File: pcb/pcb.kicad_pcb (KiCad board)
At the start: 2 copper layers, 58 parts, among them J1 Conn_02x10_Odd_Even, J2 Conn_02x03_Counter_Clockwise, Q1 BSS138, Q2 BSS138, Q3 BSS138, Q4 BSS138, SW1 SW_PUSHBUTTON, SW2 SW_PUSHBUTTON, SW3 SW_PUSHBUTTON, SW4 SW_PUSHBUTTON, U1 EFM32GG980, U2 ARDUINO_PYNQ_SHIELD, U3 IMU, U4 lidar, U5 HC-SR04, U6 HC-SR04, Y1 Crystal_GND23

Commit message: start on pcb layout
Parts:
- C1, C10, C2, C3, C4, C5, C6, C7, C8, C9, J2, L1, R5, Y1: moved to B.Cu
- J1: footprint Connector_Multicomp:Multicomp_MC9A22-2034_2x10_P2.54mm_Horizontal -> Connector_Multicomp:Multicomp_MC9A12-2034_2x10_P2.54mm_Vertical
- moved J2 142.8 mm to (117.6, 81.0)
- moved U4 122.4 mm to (94.7, 65.5), turned to 270 degrees
- moved JP9 105.1 mm to (100.3, 106.7), turned to 270 degrees
- moved JP5 105.0 mm to (73.7, 49.5), turned to 90 degrees
- moved JP3 104.6 mm to (78.7, 61.0), turned to 90 degrees
- moved U5 102.7 mm to (170.2, 65.5)
- moved R6 98.8 mm to (165.2, 68.1), turned to 180 degrees
- moved R4 96.7 mm to (127.4, 54.6)
- moved R17 96.3 mm to (127.4, 46.5)
- moved D4 95.6 mm to (133.0, 46.5), turned to 180 degrees
- moved R8 94.9 mm to (165.2, 71.6), turned to 180 degrees
- moved JP8 94.0 mm to (118.1, 106.7), turned to 270 degrees
- moved R3 92.7 mm to (127.4, 58.7)
- moved R16 92.3 mm to (127.4, 50.5)
- moved SW3 91.6 mm to (152.1, 50.5), turned to 90 degrees
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
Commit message: Add IMU footprint
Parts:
- U3: footprint localization-footprints:IMU -> Adafruit BNO055:BNO055
- moved U3 14.9 mm to (134.6, 105.4), turned to 180 degrees
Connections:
- U3 pad 6: VCC -> +3V3
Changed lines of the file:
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@@
       (net 156 "Net-(U2-PadNC1)"))
-  )
-  (module localization-footprints:IMU (layer F.Cu)
-    (at 130.302 91.186 270)
-    (fp_text reference U3 (at 0 -3.81 270) (layer F.SilkS)
-      (effects (font (size 1 1) (thickness 0.15)))
-    )
-    (fp_text value IMU (at 0 6.35 270) (layer F.Fab)
-      (effects (font (size 1 1) (thickness 0.15)))
-    )
-    (fp_line (start -8.89 5.08) (end -8.89 -2.54) (layer F.Fab) (width 0.1016))
-    (fp_line (start 8.89 5.08) (end -8.89 5.08) (layer F.Fab) (width 0.1016))
-    (fp_line (start 8.89 -2.54) (end 8.89 5.08) (layer F.Fab) (width 0.1016))
-    (fp_line (start -8.89 -2.54) (end 8.89 -2.54) (layer F.Fab) (width 0.1016))
-    (pad 1 thru_hole circle (at -7.62 -2.54 270) (size 1.524 1.524) (drill 0.762) (layers *.Cu *.Mask)
-      (net 127 /IMU/RST))
-    (pad 2 thru_hole circle (at -5.08 -2.54 270) (size 1.524 1.524) (drill 0.762) (layers *.Cu *.Mask)
-      (net 126 /IMU/SCL))
-    (pad 3 thru_hole circle (at -2.54 -2.54 270) (size 1.524 1.524) (drill 0.762) (layers *.Cu *.Mask)
-      (net 125 /IMU/SDA))
-    (pad 4 thru_hole circle (at 2.54 -2.54 270) (size 1.524 1.524) (drill 0.762) (layers *.Cu *.Mask)
-      (net 1 GND))
-    (pad 5 thru_hole circle (at 5.08 -2.54 270) (size 1.524 1.524) (drill 0.762) (layers *.Cu *.Mask)
-      (net 161 "Net-(U3-Pad5)"))
-    (pad 6 thru_hole circle (at 7.62 -2.54 270) (size 1.524 1.524) (drill 0.762) (layers *.Cu *.Mask)
-      (net 84 VCC))
-    (pad 7 thru_hole circle (at 5.08 5.08 270) (size 1.524 1.524) (drill 0.762) (layers *.Cu *.Mask)
-      (net 160 "Net-(U3-Pad7)"))
-    (pad 8 thru_hole circle (at 2.54 5.08 270) (size 1.524 1.524) (drill 0.762) (layers *.Cu *.Mask)
-      (net 159 "Net-(U3-Pad8)"))
-    (pad 9 thru_hole circle (at -2.54 5.08 270) (size 1.524 1.524) (drill 0.762) (layers *.Cu *.Mask)
-      (net 158 "Net-(U3-Pad9)"))
-    (pad 10 thru_hole circle (at -5.08 5.08 270) (size 1.524 1.524) (drill 0.762) (layers *.Cu *.Mask)
-      (net 157 "Net-(U3-Pad10)"))
   )
   (module Connector_PinHeader_2.54mm:PinHeader_1x07_P2.54mm_Vertical (layer F.Cu)
@@
     )
   )
+  (module "Adafruit BNO055:BNO055" (layer F.Cu)
+    (at 134.62 105.41 180)
+    (fp_text reference U3 (at 0 0.5 180) (layer F.SilkS)
+      (effects (font (size 1 1) (thickness 0.15)))
+    )
+    (fp_text value IMU (at 0 -0.5 180) (layer F.Fab)
+      (effects (font (size 1 1) (thickness 0.15)))
+    )
+    (pad 1 thru_hole circle (at 7.62 15.24 180) (size 1.524 1.524) (drill 0.762) (layers *.Cu *.Mask)
+      (net 127 /IMU/RST))
+    (pad 2 thru_hole circle (at 5.08 15.24 180) (size 1.524 1.524) (drill 0.762) (layers *.Cu *.Mask)
+      (net 126 /IMU/SCL))
+    (pad 3 thru_hole circle (at 2.54 15.24 180) (size 1.524 1.524) (drill 0.762) (layers *.Cu *.Mask)
+      (net 125 /IMU/SDA))
+    (pad 4 thru_hole circle (at 0 15.24 180) (size 1.524 1.524) (drill 0.762) (layers *.Cu *.Mask)
+      (net 1 GND))
+    (pad 5 thru_hole circle (at -2.54 15.24 180) (size 1.524 1.524) (drill 0.762) (layers *.Cu *.Mask)
+      (net 161 "Net-(U3-Pad5)"))
+    (pad 6 thru_hole circle (at -5.08 15.24 180) (size 1.524 1.524) (drill 0.762) (layers *.Cu *.Mask)
+      (net 2 +3V3))
+    (pad 7 thru_hole circle (at -2.54 -2.54 180) (size 1.524 1.524) (drill 0.762) (layers *.Cu *.Mask)
+      (net 160 "Net-(U3-Pad7)"))
+    (pad 8 thru_hole circle (at 0 -2.54 180) (size 1.524 1.524) (drill 0.762) (layers *.Cu *.Mask)
+      (net 159 "Net-(U3-Pad8)"))
+    (pad 9 thru_hole circle (at 2.54 -2.54 180) (size 1.524 1.524) (drill 0.762) (layers *.Cu *.Mask)
+      (net 158 "Net-(U3-Pad9)"))
+    (pad 10 thru_hole circle (at 5.08 -2.54 180) (size 1.524 1.524) (drill 0.762) (layers *.Cu *.Mask)
+      (net 157 "Net-(U3-Pad10)"))
+  )
 )

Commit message: continue on pcb
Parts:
- added BT1: Battery, Connector_PinHeader_2.54mm:PinHeader_1x02_P2.54mm_Vertical, F.Cu at (59.9, 49.3)
- added C11: 10μF, Capacitor_SMD:C_1206_3216Metric_Pad1.42x1.75mm_HandSolder, F.Cu at (65.0, 59.4)
- added C12: 1μF, Capacitor_SMD:C_1206_3216Metric_Pad1.42x1.75mm_HandSolder, F.Cu at (68.6, 59.5)
- added C13: 100nF, Capacitor_SMD:C_1206_3216Metric_Pad1.42x1.75mm_HandSolder, F.Cu at (72.6, 59.4)
- added J3: Conn_01x03_Female, Connector_PinSocket_2.54mm:PinSocket_1x03_P2.54mm_Vertical, F.Cu at (61.5, 107.7)
- added JP10: Jumper_NC_Dual, Connector_PinHeader_2.54mm:PinHeader_1x03_P2.54mm_Vertical, F.Cu at (59.9, 55.4)
- added U7: HC-SR04, Connector_PinHeader_2.54mm:PinHeader_1x04_P2.54mm_Vertical, F.Cu at (171.7, 46.7)
- added U8: HC-SR04, Connector_PinHeader_2.54mm:PinHeader_1x04_P2.54mm_Vertical, F.Cu at (172.2, 100.1)
- C1, C10, C2, C3, C4, C5, C6, C7, C8, C9: footprint Capacitor_SMD:C_0603_1608Metric_Pad1.05x0.95mm_HandSolder -> Capacitor_SMD:C_1206_3216Metric_Pad1.42x1.75mm_HandSolder
- D1, D2, D3, D4: footprint LED_SMD:LED_0603_1608Metric_Pad1.05x0.95mm_HandSolder -> LED_SMD:LED_1206_3216Metric_Pad1.42x1.75mm_HandSolder
- L1: footprint Inductor_SMD:L_0603_1608Metric_Pad1.05x0.95mm_HandSolder -> Inductor_SMD:L_1206_3216Metric_Pad1.42x1.75mm_HandSolder
- R1, R10, R11, R12, R13, R14, R15, R16, R17, R2, R3, R4, R5, R6, R7, R8, R9: footprint Resistor_SMD:R_0603_1608Metric_Pad1.05x0.95mm_HandSolder -> Resistor_SMD:R_1206_3216Metric_Pad1.42x1.75mm_HandSolder
- moved U4 40.3 mm to (59.9, 85.9), turned to 180 degrees
- moved C1 25.7 mm to (105.8, 67.3)
- moved C2 22.6 mm to (112.8, 69.6)
- moved U5 21.3 mm to (159.7, 47.0), turned to 90 degrees
- moved SW1 21.1 mm to (151.6, 62.4)
- moved SW2 20.5 mm to (143.5, 62.4)
- moved R8 18.1 mm to (166.6, 53.5), turned to 270 degrees
- moved R11 17.2 mm to (167.2, 88.6), turned to 270 degrees
- moved Q2 16.9 mm to (167.9, 58.4), turned to 90 degrees
- moved R13 16.3 mm to (161.7, 88.6), turned to 270 degrees
- moved R15 16.2 mm to (126.5, 67.6)
- moved R1 15.4 mm to (126.5, 75.7)
- moved C5 14.9 mm to (112.8, 74.2)
- moved R9 14.9 mm to (167.9, 65.2), turned to 90 degrees
- moved R2 14.9 mm to (126.5, 71.6)
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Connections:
- J2 pad 1: /SPI/MISO -> Net-(J2-Pad1)
- J2 pad 2: /SPI/SCLK -> /SPI/SS
- J2 pad 3: /SPI/SS -> /SPI/MOSI
- J2 pad 4: Net-(J2-Pad4) -> /SPI/SCLK
- J2 pad 5: /SPI/MOSI -> Net-(J2-Pad5)
- J2 pad 6: Net-(J2-Pad6) -> /SPI/MISO
- U1 pad 3: /EFM_DEBUG/SW_1 -> /EFM_DEBUG/SW_2
- U1 pad 4: /EFM_DEBUG/SW_2 -> /EFM_DEBUG/SW_1
- U1 pad 51: /LIDAR/MOTO_CTRL -> Net-(U1-Pad51)
- U1 pad 70: Net-(U1-Pad70) -> /LIDAR/MOTO_CTRL
- U4 pad 5: VCC -> Net-(C11-Pad1)
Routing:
- net /PYNQ-DEBUG/SW_2: track 0.00 -> 83.8 mm
- net /PYNQ-DEBUG/SW_1: track 0.00 -> 62.5 mm
- net /EFM_DEBUG/SW_1: track 0.00 -> 25.3 mm
- net Net-(JP1-Pad6): track 0.00 -> 20.0 mm
- net Net-(JP1-Pad5): track 0.00 -> 18.2 mm
- net /JTAG/SWDIO: track 0.00 -> 17.7 mm
- net Net-(JP1-Pad4): track 0.00 -> 16.5 mm
- net /JTAG/SWCLK: track 0.00 -> 16.4 mm
- net /EFM_DEBUG/SW_2: track 0.00 -> 15.5 mm
- net Net-(JP1-Pad3): track 0.00 -> 14.8 mm
- net Net-(JP1-Pad2): track 0.00 -> 13.0 mm
- net Net-(C11-Pad1): track 0.00 -> 12.7 mm
- net Net-(JP1-Pad1): track 0.00 -> 11.6 mm
- net GND: track 0.00 -> 7.27 mm
- net Net-(BT1-Pad1): track 0.00 -> 6.10 mm
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
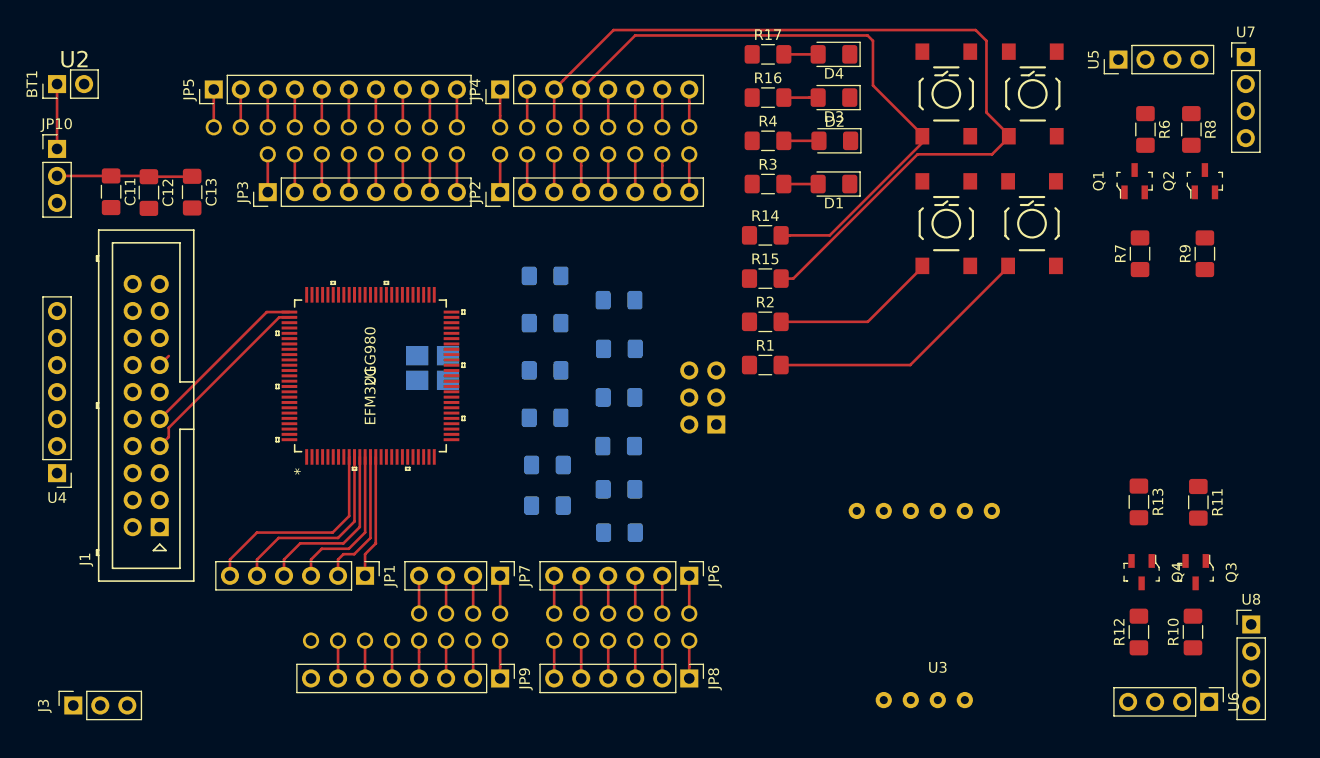
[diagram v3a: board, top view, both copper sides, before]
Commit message: Add level shifters and jumpers and new gpio
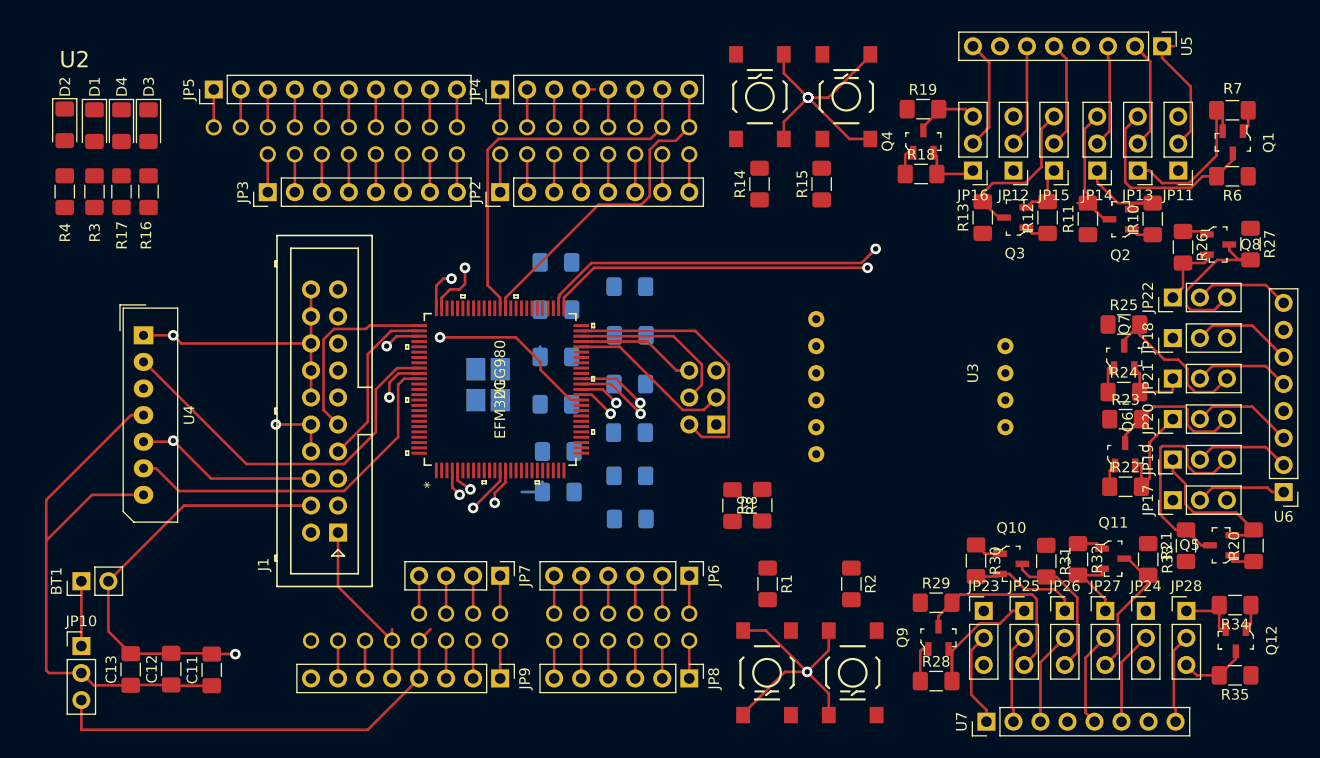
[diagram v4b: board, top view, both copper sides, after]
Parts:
- removed J3: Conn_01x03_Female, Connector_PinSocket_2.54mm:PinSocket_1x03_P2.54mm_Vertical
- removed JP1: M06, Connector_PinHeader_2.54mm:PinHeader_1x06_P2.54mm_Vertical
- removed U8: HC-SR04, Connector_PinHeader_2.54mm:PinHeader_1x04_P2.54mm_Vertical
- added JP11: Jumper_NC_Dual, Connector_PinHeader_2.54mm:PinHeader_1x03_P2.54mm_Vertical, F.Cu at (165.4, 57.4)
- added JP12: Jumper_NC_Dual, Connector_PinHeader_2.54mm:PinHeader_1x03_P2.54mm_Vertical, F.Cu at (149.9, 57.4)
- added JP13: Jumper_NC_Dual, Connector_PinHeader_2.54mm:PinHeader_1x03_P2.54mm_Vertical, F.Cu at (161.5, 57.4)
- added JP14: Jumper_NC_Dual, Connector_PinHeader_2.54mm:PinHeader_1x03_P2.54mm_Vertical, F.Cu at (157.7, 57.4)
- added JP15: Jumper_NC_Dual, Connector_PinHeader_2.54mm:PinHeader_1x03_P2.54mm_Vertical, F.Cu at (153.7, 57.4)
- added JP16: Jumper_NC_Dual, Connector_PinHeader_2.54mm:PinHeader_1x03_P2.54mm_Vertical, F.Cu at (146.1, 57.4)
- added JP17: Jumper_NC_Dual, Connector_PinHeader_2.54mm:PinHeader_1x03_P2.54mm_Vertical, F.Cu at (164.8, 88.4)
- added JP18: Jumper_NC_Dual, Connector_PinHeader_2.54mm:PinHeader_1x03_P2.54mm_Vertical, F.Cu at (164.8, 73.2)
- added JP19: Jumper_NC_Dual, Connector_PinHeader_2.54mm:PinHeader_1x03_P2.54mm_Vertical, F.Cu at (164.8, 84.6)
- added JP20: Jumper_NC_Dual, Connector_PinHeader_2.54mm:PinHeader_1x03_P2.54mm_Vertical, F.Cu at (164.8, 80.8)
- added JP21: Jumper_NC_Dual, Connector_PinHeader_2.54mm:PinHeader_1x03_P2.54mm_Vertical, F.Cu at (164.8, 77.0)
- added JP22: Jumper_NC_Dual, Connector_PinHeader_2.54mm:PinHeader_1x03_P2.54mm_Vertical, F.Cu at (164.8, 69.3)
- added JP23: Jumper_NC_Dual, Connector_PinHeader_2.54mm:PinHeader_1x03_P2.54mm_Vertical, F.Cu at (147.1, 98.8)
- added JP24: Jumper_NC_Dual, Connector_PinHeader_2.54mm:PinHeader_1x03_P2.54mm_Vertical, F.Cu at (162.3, 98.8)
- added JP25: Jumper_NC_Dual, Connector_PinHeader_2.54mm:PinHeader_1x03_P2.54mm_Vertical, F.Cu at (150.9, 98.8)
- added JP26: Jumper_NC_Dual, Connector_PinHeader_2.54mm:PinHeader_1x03_P2.54mm_Vertical, F.Cu at (154.7, 98.8)
- added JP27: Jumper_NC_Dual, Connector_PinHeader_2.54mm:PinHeader_1x03_P2.54mm_Vertical, F.Cu at (158.5, 98.8)
- added JP28: Jumper_NC_Dual, Connector_PinHeader_2.54mm:PinHeader_1x03_P2.54mm_Vertical, F.Cu at (166.1, 98.8)
- added Q10: BSS138, digikey-footprints:SOT-23-3, F.Cu at (149.6, 94.4)
- added Q11: BSS138, digikey-footprints:SOT-23-3, F.Cu at (159.2, 93.9)
- added Q12: BSS138, digikey-footprints:SOT-23-3, F.Cu at (170.8, 101.6)
- added Q5: BSS138, digikey-footprints:SOT-23-3, F.Cu at (169.4, 92.6)
- added Q6: BSS138, digikey-footprints:SOT-23-3, F.Cu at (160.4, 84.1)
- added Q7: BSS138, digikey-footprints:SOT-23-3, F.Cu at (160.3, 74.9)
- added Q8: BSS138, digikey-footprints:SOT-23-3, F.Cu at (169.1, 64.4)
- added Q9: BSS138, digikey-footprints:SOT-23-3, F.Cu at (142.8, 101.3)
- added R18: 10k, Resistor_SMD:R_1206_3216Metric_Pad1.42x1.75mm_HandSolder, F.Cu at (141.2, 57.7)
- added R19: 10k, Resistor_SMD:R_1206_3216Metric_Pad1.42x1.75mm_HandSolder, F.Cu at (141.4, 51.6)
- added R20: 10k, Resistor_SMD:R_1206_3216Metric_Pad1.42x1.75mm_HandSolder, F.Cu at (172.4, 92.7)
- added R21: 10k, Resistor_SMD:R_1206_3216Metric_Pad1.42x1.75mm_HandSolder, F.Cu at (166.1, 92.7)
- added R22: 10k, Resistor_SMD:R_1206_3216Metric_Pad1.42x1.75mm_HandSolder, F.Cu at (160.4, 87.1)
- added R23: 10k, Resistor_SMD:R_1206_3216Metric_Pad1.42x1.75mm_HandSolder, F.Cu at (160.4, 80.8)
- added R24: 10k, Resistor_SMD:R_1206_3216Metric_Pad1.42x1.75mm_HandSolder, F.Cu at (160.2, 78.2)
- added R25: 10k, Resistor_SMD:R_1206_3216Metric_Pad1.42x1.75mm_HandSolder, F.Cu at (160.2, 71.9)
- added R26: 10k, Resistor_SMD:R_1206_3216Metric_Pad1.42x1.75mm_HandSolder, F.Cu at (165.8, 64.6)
- added R27: 10k, Resistor_SMD:R_1206_3216Metric_Pad1.42x1.75mm_HandSolder, F.Cu at (172.1, 64.3)
- added R28: 10k, Resistor_SMD:R_1206_3216Metric_Pad1.42x1.75mm_HandSolder, F.Cu at (142.6, 105.4)
- added R29: 10k, Resistor_SMD:R_1206_3216Metric_Pad1.42x1.75mm_HandSolder, F.Cu at (142.6, 98.0)
- added R30: 10k, Resistor_SMD:R_1206_3216Metric_Pad1.42x1.75mm_HandSolder, F.Cu at (146.3, 94.1)
- added R31: 10k, Resistor_SMD:R_1206_3216Metric_Pad1.42x1.75mm_HandSolder, F.Cu at (152.9, 94.1)
- added R32: 10k, Resistor_SMD:R_1206_3216Metric_Pad1.42x1.75mm_HandSolder, F.Cu at (155.9, 94.0)
- added R33: 10k, Resistor_SMD:R_1206_3216Metric_Pad1.42x1.75mm_HandSolder, F.Cu at (162.5, 94.0)
- added R34: 10k, Resistor_SMD:R_1206_3216Metric_Pad1.42x1.75mm_HandSolder, F.Cu at (170.7, 98.3)
- added R35: 10k, Resistor_SMD:R_1206_3216Metric_Pad1.42x1.75mm_HandSolder, F.Cu at (170.7, 104.9)
- R8: value 10k -> 2.2k
- R9: value 10k -> 4.7k
- U4: footprint Connector_PinHeader_2.54mm:PinHeader_1x07_P2.54mm_Vertical -> Connector_Molex:Molex_SPOX_5267-07A_1x07_P2.50mm_Vertical
- U5, U6, U7: value HC-SR04 -> ULTRASONIC-GPIO; footprint Connector_PinHeader_2.54mm:PinHeader_1x04_P2.54mm_Vertical -> Connector_PinHeader_2.54mm:PinHeader_1x08_P2.54mm_Vertical
- moved D2 72.4 mm to (60.7, 53.1), turned to 270 degrees
- moved D1 69.7 mm to (63.5, 53.2), turned to 270 degrees
- moved D4 67.3 mm to (66.0, 53.2), turned to 270 degrees
- moved U7 67.1 mm to (147.3, 109.2), turned to 90 degrees
- moved R4 66.3 mm to (60.7, 59.4), turned to 90 degrees
- moved D3 64.5 mm to (68.5, 53.2), turned to 270 degrees
- moved R3 63.3 mm to (63.5, 59.4), turned to 90 degrees
- moved R17 62.1 mm to (66.0, 59.4), turned to 90 degrees
- moved R16 58.9 mm to (68.5, 59.4), turned to 90 degrees
- moved R8 55.8 mm to (123.4, 88.9)
- moved SW1 49.0 mm to (126.7, 104.6), turned to 270 degrees
- moved R9 47.9 mm to (126.2, 88.9)
- moved JP10 46.8 mm to (62.2, 102.1)
- moved BT1 46.8 mm to (62.2, 96.0)
- moved C11 45.9 mm to (74.5, 104.4), turned to 90 degrees
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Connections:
- net Net-(U3-Pad9) renamed /IMU/INT
- Q1 pad 2: /OLD-SONAR/TRIG_1 -> /PD5
- Q1 pad 3: Net-(Q1-Pad3) -> Net-(JP13-Pad3)
- Q2 pad 2: /OLD-SONAR/ECHO_1 -> /PD6
- Q2 pad 3: Net-(Q2-Pad3) -> Net-(JP14-Pad3)
- Q3 pad 2: /OLD-SONAR/TRIG_2 -> /PF11
- Q3 pad 3: Net-(Q3-Pad3) -> Net-(JP15-Pad3)
- Q4 pad 2: /OLD-SONAR/ECHO_2 -> /PF10
- Q4 pad 3: Net-(Q4-Pad3) -> Net-(JP16-Pad3)
- R10 pad 1: VCC -> +3V3
- R10 pad 2: Net-(Q3-Pad3) -> /PD6
- R11 pad 1: +3V3 -> VCC
- R11 pad 2: /OLD-SONAR/TRIG_2 -> Net-(JP14-Pad3)
- R12 pad 1: VCC -> +3V3
- R12 pad 2: Net-(Q4-Pad3) -> /PF11
- R13 pad 1: +3V3 -> VCC
- R13 pad 2: /OLD-SONAR/ECHO_2 -> Net-(JP15-Pad3)
- R6 pad 2: Net-(Q1-Pad3) -> Net-(JP13-Pad3)
- R7 pad 2: /OLD-SONAR/TRIG_1 -> /PD5
- R8 pad 1: VCC -> +3V3
- R8 pad 2: Net-(Q2-Pad3) -> /IMU/SDA
- R9 pad 2: /OLD-SONAR/ECHO_1 -> /IMU/SCL
- U1 pad 13: Net-(JP1-Pad2) -> /PB4
- U1 pad 14: Net-(JP1-Pad1) -> /PB5
- U1 pad 22: Net-(U1-Pad22) -> /IMU/SDA
- U1 pad 23: Net-(U1-Pad23) -> /IMU/SCL
- U1 pad 24: Net-(U1-Pad24) -> /IMU/RST
- U1 pad 26: /OLD-SONAR/TRIG_1 -> Net-(U1-Pad26)
- U1 pad 27: /OLD-SONAR/ECHO_1 -> Net-(U1-Pad27)
- U1 pad 28: /OLD-SONAR/TRIG_2 -> Net-(U1-Pad28)
- U1 pad 29: /OLD-SONAR/ECHO_2 -> Net-(U1-Pad29)
- U1 pad 3: /EFM_DEBUG/SW_2 -> Net-(U1-Pad3)
- U1 pad 37: Net-(U1-Pad37) -> /PB9
- U1 pad 38: Net-(U1-Pad38) -> /PB10
- U1 pad 39: /PYNQ_SDA -> /PB11
- U1 pad 4: /EFM_DEBUG/SW_1 -> /PA3
- U1 pad 40: /PYNQ_SCL -> /PB12
- U1 pad 46: Net-(U1-Pad46) -> /SPI/MOSI
- U1 pad 47: Net-(U1-Pad47) -> /SPI/MISO
- U1 pad 48: Net-(U1-Pad48) -> /SPI/SCLK
- U1 pad 49: Net-(U1-Pad49) -> /SPI/SS
- U1 pad 5: Net-(U1-Pad5) -> /PA4
- U1 pad 51: Net-(U1-Pad51) -> /PD5
- U1 pad 52: /IMU/SDA -> /PD6
- U1 pad 53: /IMU/SCL -> Net-(U1-Pad53)
- U1 pad 54: /IMU/RST -> Net-(U1-Pad54)
- U1 pad 55: Net-(U1-Pad55) -> /PYNQ_SDA
- U1 pad 56: Net-(U1-Pad56) -> /PYNQ_SCL
- U1 pad 60: /PYNQ_RX -> Net-(U1-Pad60)
- U1 pad 61: /PYNQ_TX -> Net-(U1-Pad61)
- U1 pad 62: /LIDAR/RX -> /PYNQ_RX
- U1 pad 63: /LIDAR/TX -> /PYNQ_TX
- U1 pad 64: /SPI/SS -> Net-(U1-Pad64)
- U1 pad 65: /SPI/SCLK -> Net-(U1-Pad65)
- U1 pad 66: /SPI/MISO -> Net-(U1-Pad66)
- U1 pad 67: /SPI/MOSI -> Net-(U1-Pad67)
- U1 pad 70: /LIDAR/MOTO_CTRL -> Net-(U1-Pad70)
- U1 pad 74: Net-(U1-Pad74) -> /PF10
- U1 pad 75: Net-(U1-Pad75) -> /PF11
- U1 pad 84: Net-(U1-Pad84) -> /LIDAR/TX
- U1 pad 85: Net-(U1-Pad85) -> /LIDAR/RX
- U1 pad 86: Net-(U1-Pad86) -> /LIDAR/MOTO_CTRL
- U1 pad 89: Net-(JP2-Pad1) -> Net-(U1-Pad89)
- U1 pad 90: Net-(JP2-Pad2) -> Net-(U1-Pad90)
- U1 pad 91: Net-(JP2-Pad3) -> Net-(U1-Pad91)
- U1 pad 92: Net-(JP2-Pad4) -> Net-(U1-Pad92)
- U4 pad 2: VCC -> /LIDAR/TX
- U4 pad 4: /LIDAR/TX -> Net-(C11-Pad1)
- U4 pad 5: Net-(C11-Pad1) -> GND
- U4 pad 7: GND -> Net-(C11-Pad1)
- U5 pad 1: VCC -> Net-(JP11-Pad2)
- U5 pad 2: Net-(Q1-Pad3) -> Net-(JP13-Pad2)
- U5 pad 3: Net-(Q2-Pad3) -> Net-(JP14-Pad2)
- U6 pad 1: VCC -> Net-(JP17-Pad2)
- U6 pad 2: Net-(Q3-Pad3) -> Net-(JP19-Pad2)
- U6 pad 3: Net-(Q4-Pad3) -> Net-(JP20-Pad2)
- U7 pad 1: VCC -> Net-(JP23-Pad2)
- U7 pad 2: Net-(Q2-Pad3) -> Net-(JP25-Pad2)
- U7 pad 3: Net-(Q2-Pad3) -> Net-(JP26-Pad2)
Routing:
- net GND: track 7.27 -> 167.4 mm, vias 0 -> 8
- net /PA3: track 0.00 -> 83.1 mm, vias 0 -> 1
- net /PYNQ-DEBUG/SW_2: track 83.8 -> 3.56 mm
- net /PA4: track 0.00 -> 78.2 mm, vias 0 -> 1
- net /PD5: track 0.00 -> 76.7 mm, vias 0 -> 1
- net /PB4: track 0.00 -> 74.7 mm, vias 0 -> 1
- net /PB11: track 0.00 -> 72.9 mm, vias 0 -> 1
- net /PB5: track 0.00 -> 72.4 mm, vias 0 -> 1
- net /PF11: track 0.00 -> 70.1 mm, vias 0 -> 1
- net /PD6: track 0.00 -> 69.6 mm, vias 0 -> 1
- net /PB9: track 0.00 -> 68.8 mm, vias 0 -> 1
- net /PB12: track 0.00 -> 67.3 mm, vias 0 -> 1
- net /PB10: track 0.00 -> 63.8 mm, vias 0 -> 1
- net /PF10: track 0.00 -> 63.4 mm, vias 0 -> 1
- net /PYNQ-DEBUG/SW_1: track 62.5 -> 4.37 mm
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- added copper zone on GND, net GND
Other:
- copper layers 2 -> 4
- net class Default: via_dia 0.8 -> 1; via_drill 0.4 -> 0.5
- rule via_min_drill: 0.3 -> 0.5
- rule via_min_size: 0.4 -> 1
